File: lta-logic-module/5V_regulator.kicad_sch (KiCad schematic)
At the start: 10 parts

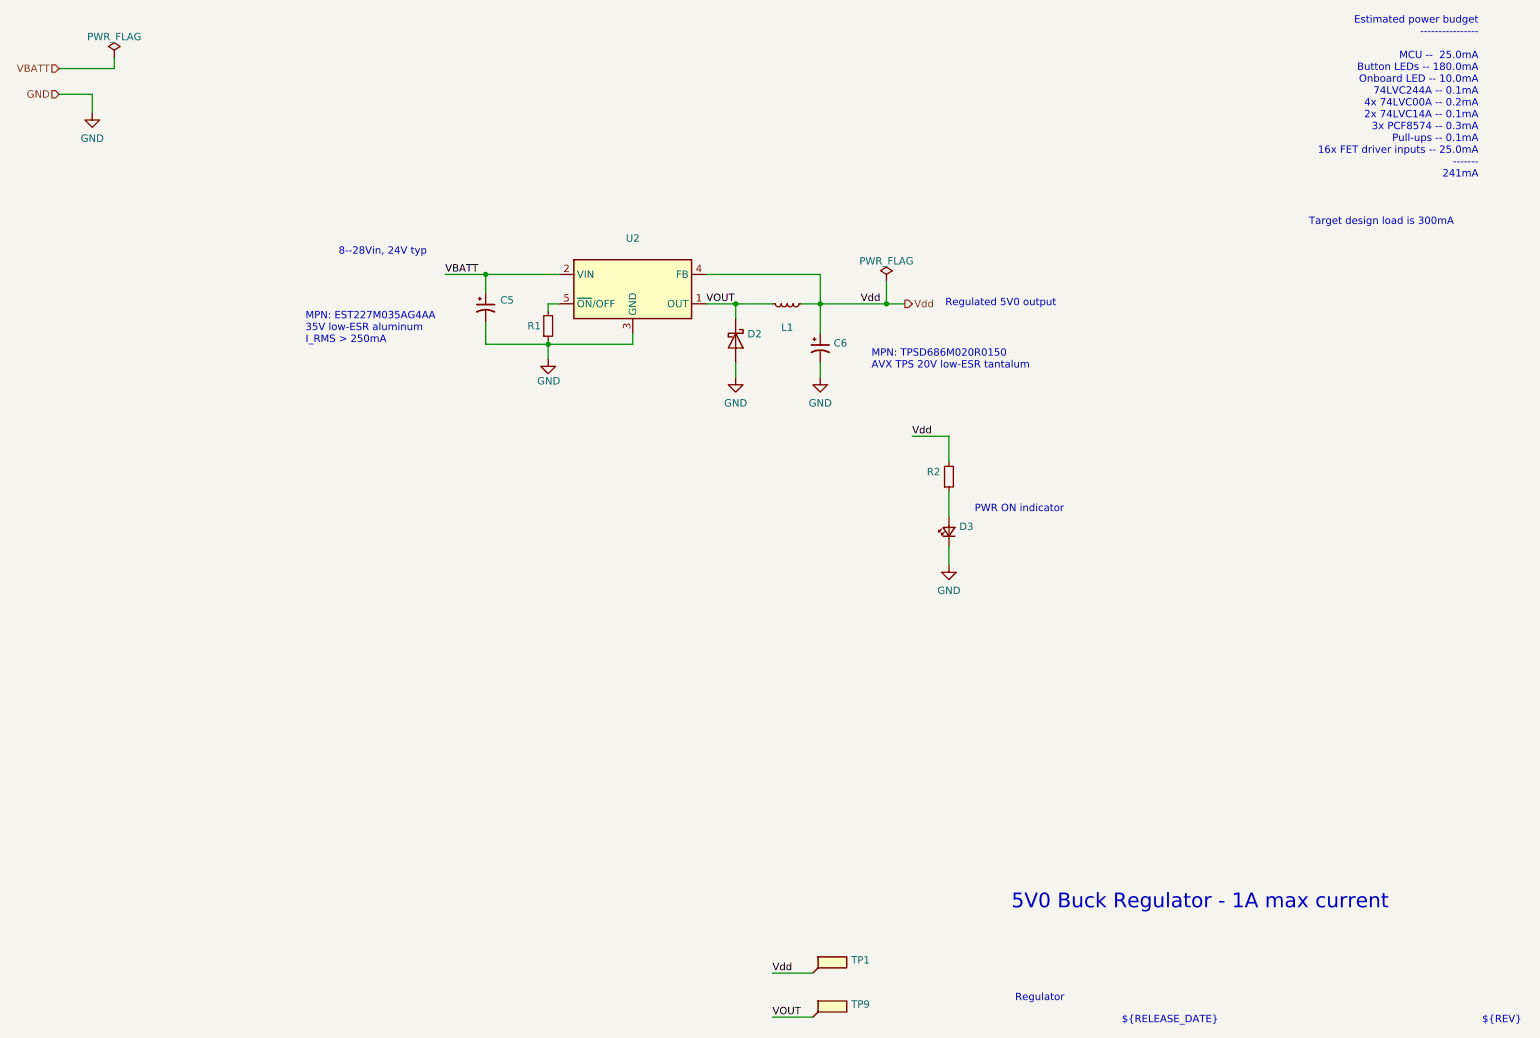
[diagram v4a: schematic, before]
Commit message: Update logic module power budget from button LED measurements.
Button LEDs draw ~11mA each (98 mA total) empirically; not the ~20mA each
I initially guessed for estimating purposes.
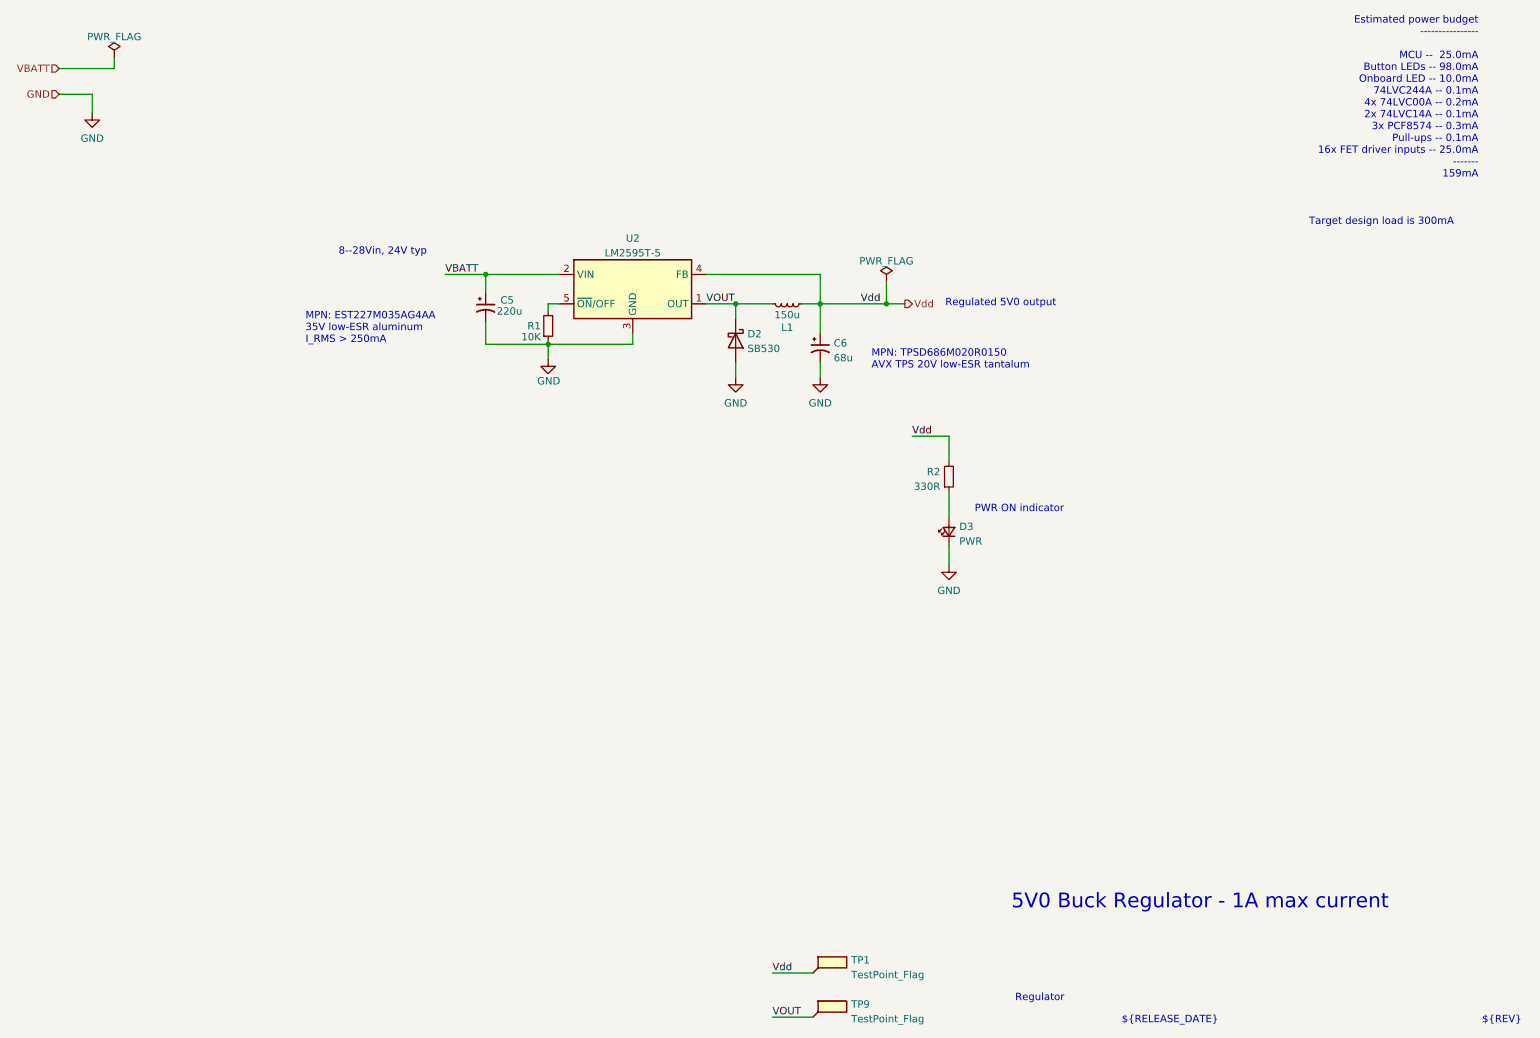
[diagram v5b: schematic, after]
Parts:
- C5: value (none) -> 220u; footprint (none) -> Capacitor_THT:CP_Radial_D8.0mm_P3.50mm
- C6: value (none) -> 68u; footprint (none) -> Capacitor_Tantalum_SMD:CP_EIA-7343-30_AVX-N
- D2: value (none) -> SB530; footprint (none) -> Diode_THT:D_DO-201AD_P15.24mm_Horizontal
- D3: value (none) -> PWR; footprint (none) -> LED_SMD:LED_0603_1608Metric
- L1: value (none) -> 150u; footprint (none) -> Aaron_THT:L_Radial_D13.5mm_P7.50mm
- R1: value (none) -> 10K; footprint (none) -> Resistor_SMD:R_0603_1608Metric
- R2: value (none) -> 330R; footprint (none) -> Resistor_SMD:R_0603_1608Metric
- TP1, TP9: value (none) -> TestPoint_Flag; footprint (none) -> Aaron_THT:TestPoint_THTPad_1.0x1.0mm_Drill0.3mm
- U2: value (none) -> LM2595T-5; footprint (none) -> Aaron_THT:TO-220-5_P3.4x3.7mm_StaggerOdd_Lead3.8mm_Vertical-SilkFix
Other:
- note added: "Estimated power budget ---------------- MCU -- 25.0mA Button LEDs -- 98.0mA Onboard LED -- 10.0mA 74LVC244A -- 0.1mA 4x 74LVC00A -- 0.2mA 2x 74LVC14A -- 0.1mA 3x PCF8574 -- 0.3mA Pull-ups -- 0.1mA 16x FET driver inputs -- 25.0mA ------- 159mA"
- note removed: "Estimated power budget ---------------- MCU -- 25.0mA Button LEDs -- 180.0mA Onboard LED -- 10.0mA 74LVC244A -- 0.1mA 4x 74LVC00A -- 0.2mA 2x 74LVC14A -- 0.1mA 3x PCF8574 -- 0.3mA Pull-ups -- 0.1mA 16x FET driver inputs -- 25.0mA ------- 241mA"
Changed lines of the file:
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@@
     (effects (font (size 1.27 1.27)) (justify left bottom))
   )
-  (text "Estimated power budget\n----------------\n\nMCU --  25.0mA\nButton LEDs -- 180.0mA\nOnboard LED -- 10.0mA\n74LVC244A -- 0.1mA\n4x 74LVC00A -- 0.2mA\n2x 74LVC14A -- 0.1mA\n3x PCF8574 -- 0.3mA\nPull-ups -- 0.1mA\n16x FET driver inputs -- 25.0mA\n-------\n241mA"
+  (text "Estimated power budget\n----------------\n\nMCU --  25.0mA\nButton LEDs -- 98.0mA\nOnboard LED -- 10.0mA\n74LVC244A -- 0.1mA\n4x 74LVC00A -- 0.2mA\n2x 74LVC14A -- 0.1mA\n3x PCF8574 -- 0.3mA\nPull-ups -- 0.1mA\n16x FET driver inputs -- 25.0mA\n-------\n159mA"
     (at 267.97 48.26 0)
     (effects (font (size 1.27 1.27)) (justify right bottom))
@@
       (effects (font (size 1.27 1.27)) (justify right))
     )
-    (property "Value" "" (id 1) (at 106.045 75.565 0)
-      (effects (font (size 1.27 1.27)) (justify right))
-    )
-    (property "Footprint" "" (id 2) (at 107.315 73.66 0)
+    (property "Value" "10K" (id 1) (at 106.045 75.565 0)
+      (effects (font (size 1.27 1.27)) (justify right))
+    )
+    (property "Footprint" "Resistor_SMD:R_0603_1608Metric" (id 2) (at 107.315 73.66 0)
       (effects (font (size 1.27 1.27)) hide)
     )
@@
       (effects (font (size 1.27 1.27)) (justify left))
     )
-    (property "Value" "" (id 1) (at 98.425 71.12 0)
-      (effects (font (size 1.27 1.27)) (justify left))
-    )
-    (property "Footprint" "" (id 2) (at 96.52 70.485 0)
+    (property "Value" "220u" (id 1) (at 98.425 71.12 0)
+      (effects (font (size 1.27 1.27)) (justify left))
+    )
+    (property "Footprint" "Capacitor_THT:CP_Radial_D8.0mm_P3.50mm" (id 2) (at 96.52 70.485 0)
       (effects (font (size 1.27 1.27)) hide)
     )
@@
     (in_bom yes) (on_board yes)
     (property "Reference" "L1" (id 0) (at 148.59 73.9308 90))
-    (property "Value" "" (id 1) (at 148.59 71.755 90))
-    (property "Footprint" "" (id 2) (at 148.59 69.85 0)
+    (property "Value" "150u" (id 1) (at 148.59 71.755 90))
+    (property "Footprint" "Aaron_THT:L_Radial_D13.5mm_P7.50mm" (id 2) (at 148.59 69.85 0)
       (effects (font (size 1.27 1.27)) hide)
     )
@@
       (effects (font (size 1.27 1.27)) (justify left))
     )
-    (property "Value" "" (id 1) (at 141.732 77.5847 90)
-      (effects (font (size 1.27 1.27)) (justify left))
-    )
-    (property "Footprint" "" (id 2) (at 139.7 76.2 0)
+    (property "Value" "SB530" (id 1) (at 141.732 77.5847 90)
+      (effects (font (size 1.27 1.27)) (justify left))
+    )
+    (property "Footprint" "Diode_THT:D_DO-201AD_P15.24mm_Horizontal" (id 2) (at 139.7 76.2 0)
       (effects (font (size 1.27 1.27)) hide)
     )
@@
       (effects (font (size 1.27 1.27)) (justify right))
     )
-    (property "Value" "" (id 1) (at 175.0314 101.3972 0)
-      (effects (font (size 1.27 1.27)) (justify right))
-    )
-    (property "Footprint" "" (id 2) (at 176.53 99.695 0)
+    (property "Value" "330R" (id 1) (at 175.0314 101.3972 0)
+      (effects (font (size 1.27 1.27)) (justify right))
+    )
+    (property "Footprint" "Resistor_SMD:R_0603_1608Metric" (id 2) (at 176.53 99.695 0)
       (effects (font (size 1.27 1.27)) hide)
     )
@@
       (effects (font (size 1.27 1.27)) (justify left))
     )
-    (property "Value" "" (id 1) (at 159.639 193.3452 0)
-      (effects (font (size 1.27 1.27)) (justify left))
-    )
-    (property "Footprint" "" (id 2) (at 158.115 193.04 0)
+    (property "Value" "TestPoint_Flag" (id 1) (at 159.639 193.3452 0)
+      (effects (font (size 1.27 1.27)) (justify left))
+    )
+    (property "Footprint" "Aaron_THT:TestPoint_THTPad_1.0x1.0mm_Drill0.3mm" (id 2) (at 158.115 193.04 0)
       (effects (font (size 1.27 1.27)) hide)
     )
@@
     (in_bom yes) (on_board yes) (fields_autoplaced)
     (property "Reference" "U2" (id 0) (at 121.92 58.5302 0))
-    (property "Value" "" (id 1) (at 121.92 61.0671 0))
-    (property "Footprint" "" (id 2) (at 123.19 73.66 0)
+    (property "Value" "LM2595T-5" (id 1) (at 121.92 61.0671 0))
+    (property "Footprint" "Aaron_THT:TO-220-5_P3.4x3.7mm_StaggerOdd_Lead3.8mm_Vertical-SilkFix" (id 2) (at 123.19 73.66 0)
       (effects (font (size 1.27 1.27) italic) (justify left) hide)
     )
@@
       (effects (font (size 1.27 1.27)) (justify left))
     )
-    (property "Value" "" (id 1) (at 156.6291 79.1785 0)
-      (effects (font (size 1.27 1.27)) (justify left))
-    )
-    (property "Footprint" "" (id 2) (at 154.305 77.47 0)
+    (property "Value" "68u" (id 1) (at 156.6291 79.1785 0)
+      (effects (font (size 1.27 1.27)) (justify left))
+    )
+    (property "Footprint" "Capacitor_Tantalum_SMD:CP_EIA-7343-30_AVX-N" (id 2) (at 154.305 77.47 0)
       (effects (font (size 1.27 1.27)) hide)
     )
@@
       (effects (font (size 1.27 1.27)) (justify left))
     )
-    (property "Value" "" (id 1) (at 159.639 185.7252 0)
-      (effects (font (size 1.27 1.27)) (justify left))
-    )
-    (property "Footprint" "" (id 2) (at 158.115 185.42 0)
+    (property "Value" "TestPoint_Flag" (id 1) (at 159.639 185.7252 0)
+      (effects (font (size 1.27 1.27)) (justify left))
+    )
+    (property "Footprint" "Aaron_THT:TestPoint_THTPad_1.0x1.0mm_Drill0.3mm" (id 2) (at 158.115 185.42 0)
       (effects (font (size 1.27 1.27)) hide)
     )
@@
       (effects (font (size 1.27 1.27)) (justify right))
     )
-    (property "Value" "" (id 1) (at 178.308 110.8587 90)
-      (effects (font (size 1.27 1.27)) (justify right))
-    )
-    (property "Footprint" "" (id 2) (at 176.53 109.22 90)
-      (effects (font (size 1.27 1.27)) hide)
-    )
+    (property "Value" "PWR" (id 1) (at 178.308 110.8587 90)
+      (effects (font (size 1.27 1.27)) (justify right))
+    )
+    (property "Footprint" "LED_SMD:LED_0603_1608Metric" (id 2) (at 176.53 109.22 90)
+      (effects (font (size 1.27 1.27)) hide)
+    )
